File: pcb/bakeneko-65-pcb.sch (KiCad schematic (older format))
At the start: 18 parts, among them J1 JST SH 4-pin, J2 AVR-ISP-6, SW1 Reset, U1 USBLC6-2SC6, U2 ATmega32U4-AU, Y1 16MHz

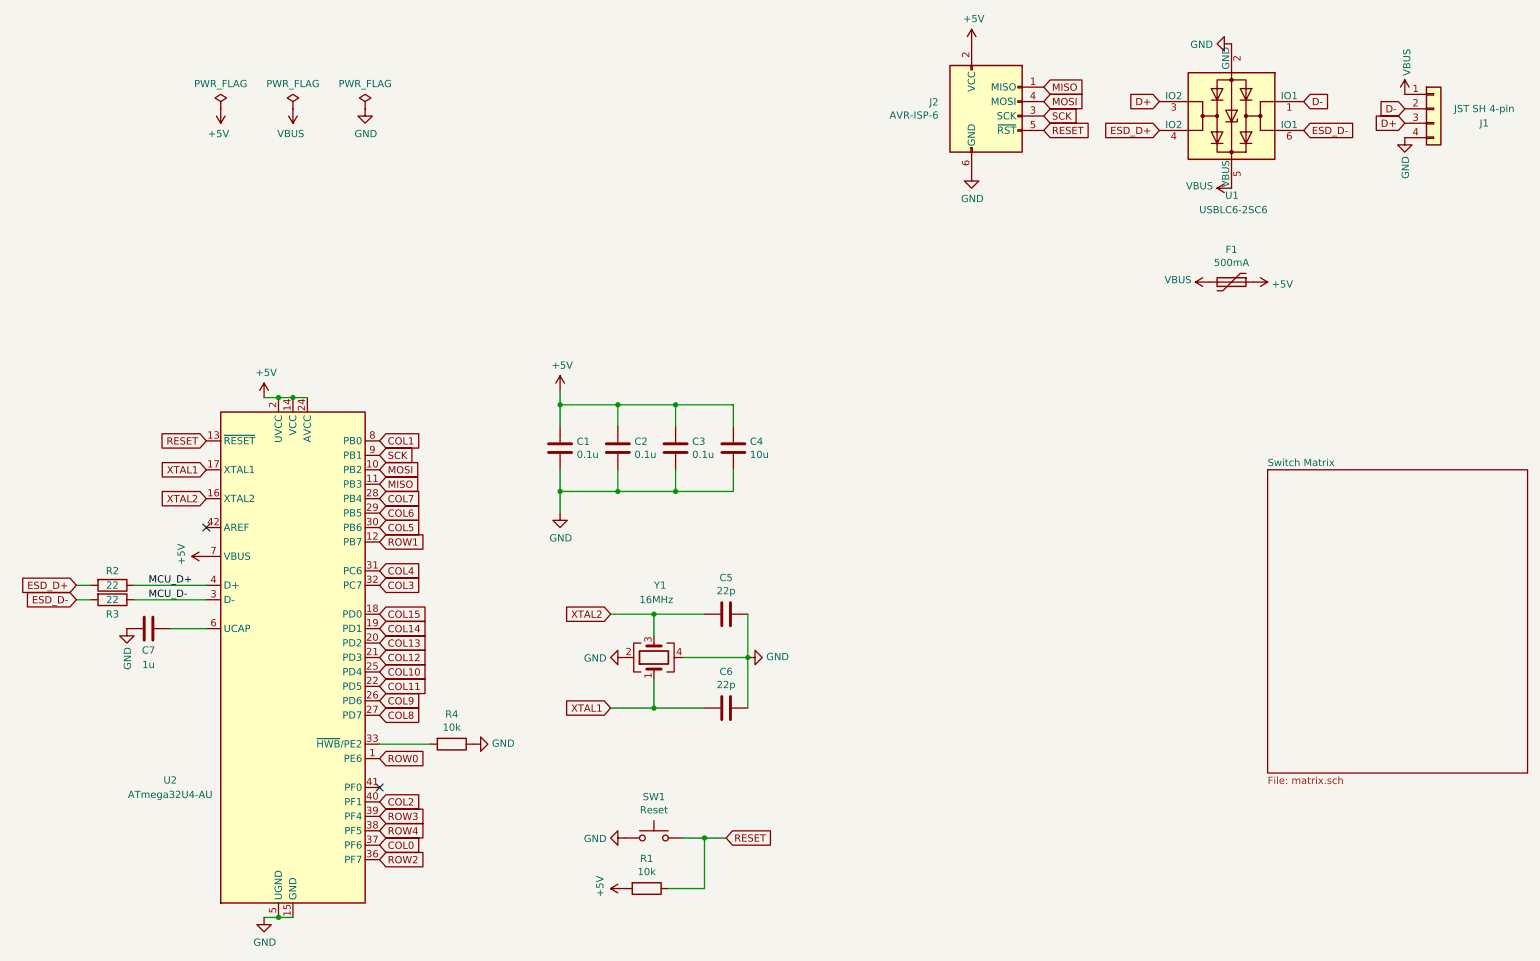
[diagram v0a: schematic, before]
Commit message: Remove ISP
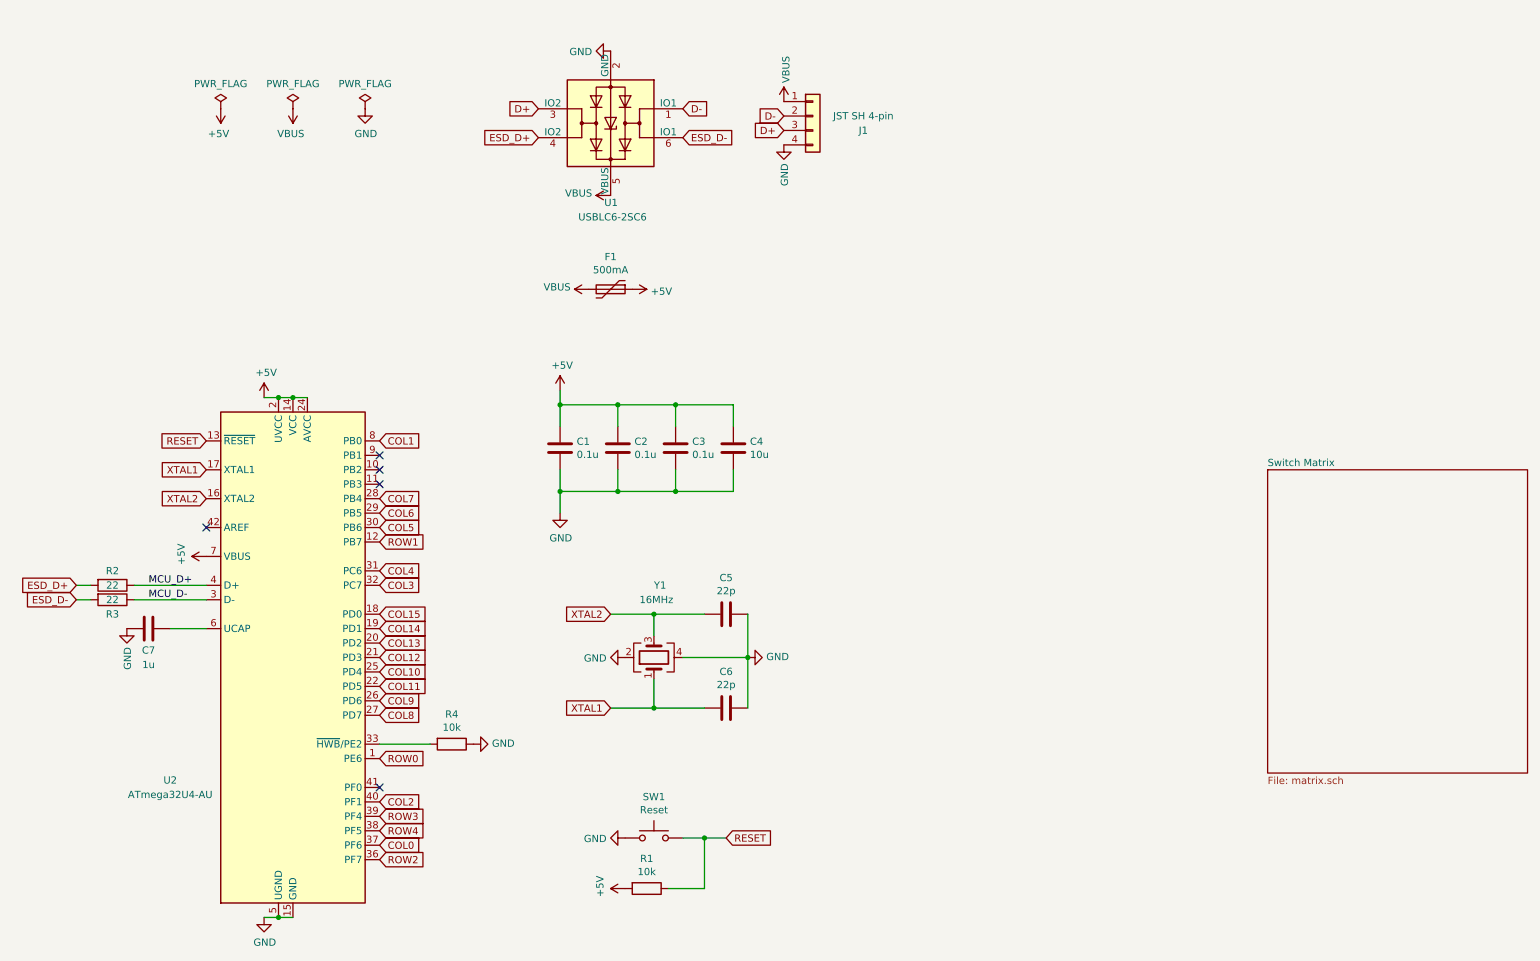
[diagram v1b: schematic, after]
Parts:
- removed J2: AVR-ISP-6, random-keyboard-parts:Reset_Pretty, symbol Connector:AVR-ISP-6
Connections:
- net MISO: no longer names the net of U2.11 (PB3)
- net MOSI: no longer names the net of U2.10 (PB2)
- net SCK: no longer names the net of U2.9 (PB1)
- no-connect marks 2 -> 5
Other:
- moved on the sheet: F1, J1, U1
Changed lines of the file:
@@
 L Device:Polyfuse F1
 U 1 1 5F2505EB
-P 8850 2800
-F 0 "F1" V 8625 2800 50  0000 C CNN
-F 1 "500mA" V 8716 2800 50  0000 C CNN
-F 2 "Fuse:Fuse_1206_3216Metric" H 8900 2600 50  0001 L CNN
-F 3 "~" H 8850 2800 50  0001 C CNN
-F 4 "C70076" H 8850 2800 50  0001 C CNN "LCSC Part #"
-	1    8850 2800
+P 4550 2850
+F 0 "F1" V 4325 2850 50  0000 C CNN
+F 1 "500mA" V 4416 2850 50  0000 C CNN
+F 2 "Fuse:Fuse_1206_3216Metric" H 4600 2650 50  0001 L CNN
+F 3 "~" H 4550 2850 50  0001 C CNN
+F 4 "C70076" H 4550 2850 50  0001 C CNN "LCSC Part #"
+	1    4550 2850
 	0    1    1    0
 $EndComp
@@
 L Connector_Generic:Conn_01x04 J1
 U 1 1 5F252816
-P 10250 1600
-F 0 "J1" H 10600 1500 50  0000 C CNN
-F 1 "JST SH 4-pin" H 10600 1600 50  0000 C CNN
-F 2 "Connector_JST:JST_SH_SM04B-SRSS-TB_1x04-1MP_P1.00mm_Horizontal" H 10250 1600 50  0001 C CNN
-F 3 "~" H 10250 1600 50  0001 C CNN
-F 4 "C160404" H 10250 1600 50  0001 C CNN "LCSC Part #"
-	1    10250 1600
+P 5950 1650
+F 0 "J1" H 6300 1550 50  0000 C CNN
+F 1 "JST SH 4-pin" H 6300 1650 50  0000 C CNN
+F 2 "Connector_JST:JST_SH_SM04B-SRSS-TB_1x04-1MP_P1.00mm_Horizontal" H 5950 1650 50  0001 C CNN
+F 3 "~" H 5950 1650 50  0001 C CNN
+F 4 "C160404" H 5950 1650 50  0001 C CNN "LCSC Part #"
+	1    5950 1650
 	1    0    0    -1
 $EndComp
@@
 L power:GND #PWR017
 U 1 1 5F256D2D
-P 8850 1150
-F 0 "#PWR017" H 8850 900 50  0001 C CNN
-F 1 "GND" V 8855 1022 50  0000 R CNN
-F 2 "" H 8850 1150 50  0001 C CNN
-F 3 "" H 8850 1150 50  0001 C CNN
-	1    8850 1150
+P 4550 1200
+F 0 "#PWR017" H 4550 950 50  0001 C CNN
+F 1 "GND" V 4555 1072 50  0000 R CNN
+F 2 "" H 4550 1200 50  0001 C CNN
+F 3 "" H 4550 1200 50  0001 C CNN
+	1    4550 1200
 	0    1    1    0
 $EndComp
@@
 	0    1    1    0
 $EndComp
-Text GLabel 10050 1600 0    50   Input ~ 0
+Text GLabel 5750 1650 0    50   Input ~ 0
 D-
-Text GLabel 10050 1700 0    50   Input ~ 0
+Text GLabel 5750 1750 0    50   Input ~ 0
 D+
 $Comp
@@
 L power:VBUS #PWR08
 U 1 1 5F275D18
-P 10050 1500
-F 0 "#PWR08" H 10050 1350 50  0001 C CNN
-F 1 "VBUS" V 10065 1628 50  0000 L CNN
-F 2 "" H 10050 1500 50  0001 C CNN
-F 3 "" H 10050 1500 50  0001 C CNN
-	1    10050 1500
+P 5750 1550
+F 0 "#PWR08" H 5750 1400 50  0001 C CNN
+F 1 "VBUS" V 5765 1678 50  0000 L CNN
+F 2 "" H 5750 1550 50  0001 C CNN
+F 3 "" H 5750 1550 50  0001 C CNN
+	1    5750 1550
 	1    0    0    -1
 $EndComp
@@
 L power:VBUS #PWR020
 U 1 1 5F276E32
-P 8850 2150
-F 0 "#PWR020" H 8850 2000 50  0001 C CNN
-F 1 "VBUS" V 8865 2278 50  0000 L CNN
-F 2 "" H 8850 2150 50  0001 C CNN
-F 3 "" H 8850 2150 50  0001 C CNN
-	1    8850 2150
+P 4550 2200
+F 0 "#PWR020" H 4550 2050 50  0001 C CNN
+F 1 "VBUS" V 4565 2328 50  0000 L CNN
+F 2 "" H 4550 2200 50  0001 C CNN
+F 3 "" H 4550 2200 50  0001 C CNN
+	1    4550 2200
 	0    -1   -1   0
 $EndComp
@@
 L power:VBUS #PWR06
 U 1 1 5F277A1C
-P 8700 2800
-F 0 "#PWR06" H 8700 2650 50  0001 C CNN
-F 1 "VBUS" V 8715 2927 50  0000 L CNN
-F 2 "" H 8700 2800 50  0001 C CNN
-F 3 "" H 8700 2800 50  0001 C CNN
-	1    8700 2800
-	0    -1   -1   0
-$EndComp
-Text GLabel 8350 1550 0    50   Input ~ 0
+P 4400 2850
+F 0 "#PWR06" H 4400 2700 50  0001 C CNN
+F 1 "VBUS" V 4415 2977 50  0000 L CNN
+F 2 "" H 4400 2850 50  0001 C CNN
+F 3 "" H 4400 2850 50  0001 C CNN
+	1    4400 2850
+	0    -1   -1   0
+$EndComp
+Text GLabel 4050 1600 0    50   Input ~ 0
 D+
-Text GLabel 9350 1550 2    50   Input ~ 0
+Text GLabel 5050 1600 2    50   Input ~ 0
 D-
 $Comp
@@
 Wire Wire Line
 	5050 5400 5500 5400
-$Comp
-L Connector:AVR-ISP-6 J2
-U 1 1 5F4C9CCE
-P 7150 1650
-F 0 "J2" H 6821 1746 50  0000 R CNN
-F 1 "AVR-ISP-6" H 6821 1655 50  0000 R CNN
-F 2 "random-keyboard-parts:Reset_Pretty" V 6900 1700 50  0001 C CNN
-F 3 " ~" H 5875 1100 50  0001 C CNN
-	1    7150 1650
-	1    0    0    -1
-$EndComp
-$Comp
-L power:GND #PWR015
-U 1 1 5F4D2BF6
-P 7050 2050
-F 0 "#PWR015" H 7050 1800 50  0001 C CNN
-F 1 "GND" H 7055 1877 50  0000 C CNN
-F 2 "" H 7050 2050 50  0001 C CNN
-F 3 "" H 7050 2050 50  0001 C CNN
-	1    7050 2050
-	1    0    0    -1
-$EndComp
-Text GLabel 7550 1450 2    50   Input ~ 0
-MISO
-Text GLabel 7550 1550 2    50   Input ~ 0
-MOSI
-Text GLabel 7550 1650 2    50   Input ~ 0
-SCK
-Text GLabel 7550 1750 2    50   Input ~ 0
-RESET
-Text GLabel 2950 4200 2    50   Input ~ 0
-MISO
-Text GLabel 2950 4000 2    50   Input ~ 0
-SCK
-Text GLabel 2950 4100 2    50   Input ~ 0
-MOSI
 Text GLabel 2950 5100 2    50   Input ~ 0
 COL15
@@
 L Power_Protection:USBLC6-2SC6 U1
 U 1 1 5F25444E
-P 8850 1650
-F 0 "U1" H 8800 2200 50  0000 L CNN
-F 1 "USBLC6-2SC6" H 8600 2300 50  0000 L CNN
-F 2 "Package_TO_SOT_SMD:SOT-23-6" H 8850 1150 50  0001 C CNN
-F 3 "https://www.st.com/resource/en/datasheet/usblc6-2.pdf" H 9050 2000 50  0001 C CNN
-F 4 "C7519" H 8850 1650 50  0001 C CNN "LCSC Part #"
-	1    8850 1650
+P 4550 1700
+F 0 "U1" H 4500 2250 50  0000 L CNN
+F 1 "USBLC6-2SC6" H 4300 2350 50  0000 L CNN
+F 2 "Package_TO_SOT_SMD:SOT-23-6" H 4550 1200 50  0001 C CNN
+F 3 "https://www.st.com/resource/en/datasheet/usblc6-2.pdf" H 4750 2050 50  0001 C CNN
+F 4 "C7519" H 4550 1700 50  0001 C CNN "LCSC Part #"
+	1    4550 1700
 	-1   0    0    1
 $EndComp
@@
 L power:GND #PWR02
 U 1 1 5F253A4B
-P 10050 1800
-F 0 "#PWR02" H 10050 1550 50  0001 C CNN
-F 1 "GND" V 10055 1672 50  0000 R CNN
-F 2 "" H 10050 1800 50  0001 C CNN
-F 3 "" H 10050 1800 50  0001 C CNN
-	1    10050 1800
+P 5750 1850
+F 0 "#PWR02" H 5750 1600 50  0001 C CNN
+F 1 "GND" V 5755 1722 50  0000 R CNN
+F 2 "" H 5750 1850 50  0001 C CNN
+F 3 "" H 5750 1850 50  0001 C CNN
+	1    5750 1850
 	1    0    0    -1
 $EndComp
@@
 Wire Wire Line
 	850  4900 950  4900
-Text GLabel 9350 1750 2    50   Input ~ 0
+Text GLabel 5050 1800 2    50   Input ~ 0
 ESD_D-
-Text GLabel 8350 1750 0    50   Input ~ 0
+Text GLabel 4050 1800 0    50   Input ~ 0
 ESD_D+
 $Comp
@@
 L power:+5V #PWR0103
 U 1 1 5F3C7287
-P 9000 2800
-F 0 "#PWR0103" H 9000 2650 50  0001 C CNN
-F 1 "+5V" V 9015 2928 50  0000 L CNN
-F 2 "" H 9000 2800 50  0001 C CNN
-F 3 "" H 9000 2800 50  0001 C CNN
-	1    9000 2800
-	0    1    1    0
-$EndComp
-$Comp
-L power:+5V #PWR0104
-U 1 1 5F3D1A13
-P 7050 1150
-F 0 "#PWR0104" H 7050 1000 50  0001 C CNN
-F 1 "+5V" H 7065 1323 50  0000 C CNN
-F 2 "" H 7050 1150 50  0001 C CNN
-F 3 "" H 7050 1150 50  0001 C CNN
-	1    7050 1150
-	1    0    0    -1
+P 4700 2850
+F 0 "#PWR0103" H 4700 2700 50  0001 C CNN
+F 1 "+5V" V 4715 2978 50  0000 L CNN
+F 2 "" H 4700 2850 50  0001 C CNN
+F 3 "" H 4700 2850 50  0001 C CNN
+	1    4700 2850
+	0    1    1    0
 $EndComp
 $Comp
@@
 Text GLabel 2950 6500 2    50   Input ~ 0
 ROW3
+NoConn ~ 2950 4000
+NoConn ~ 2950 4100
+NoConn ~ 2950 4200
 $EndSCHEMATC
